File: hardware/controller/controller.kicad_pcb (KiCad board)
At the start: 2 copper layers, 64 x 39 mm, 13 parts, among them J1 Conn_01x02_Pin, J2 Conn_01x02_Pin, J3 Conn_01x02_Pin, J4 Conn_01x02_Pin, SW1 SW_DIP_x01, U1 ESP32-S3-DEVKITC-1-N8R8

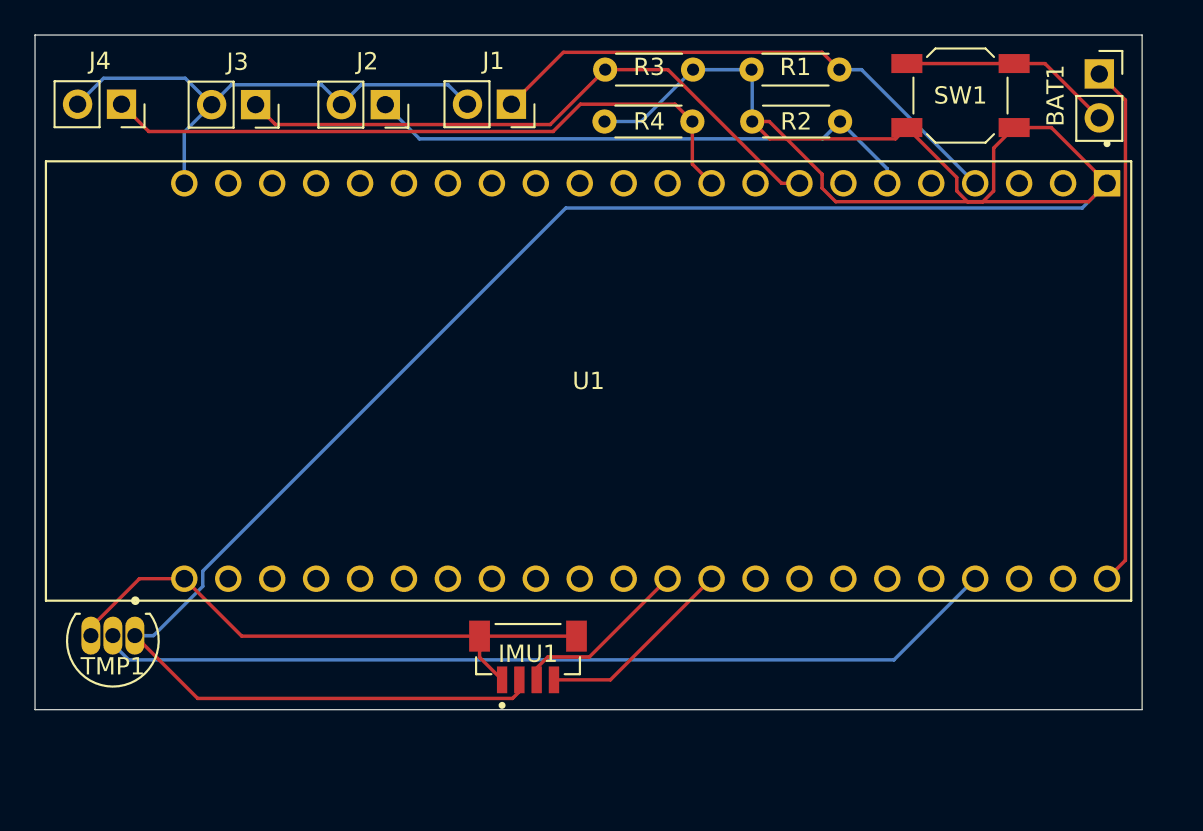
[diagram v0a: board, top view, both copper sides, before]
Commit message: PCB Redesign for UWB Module
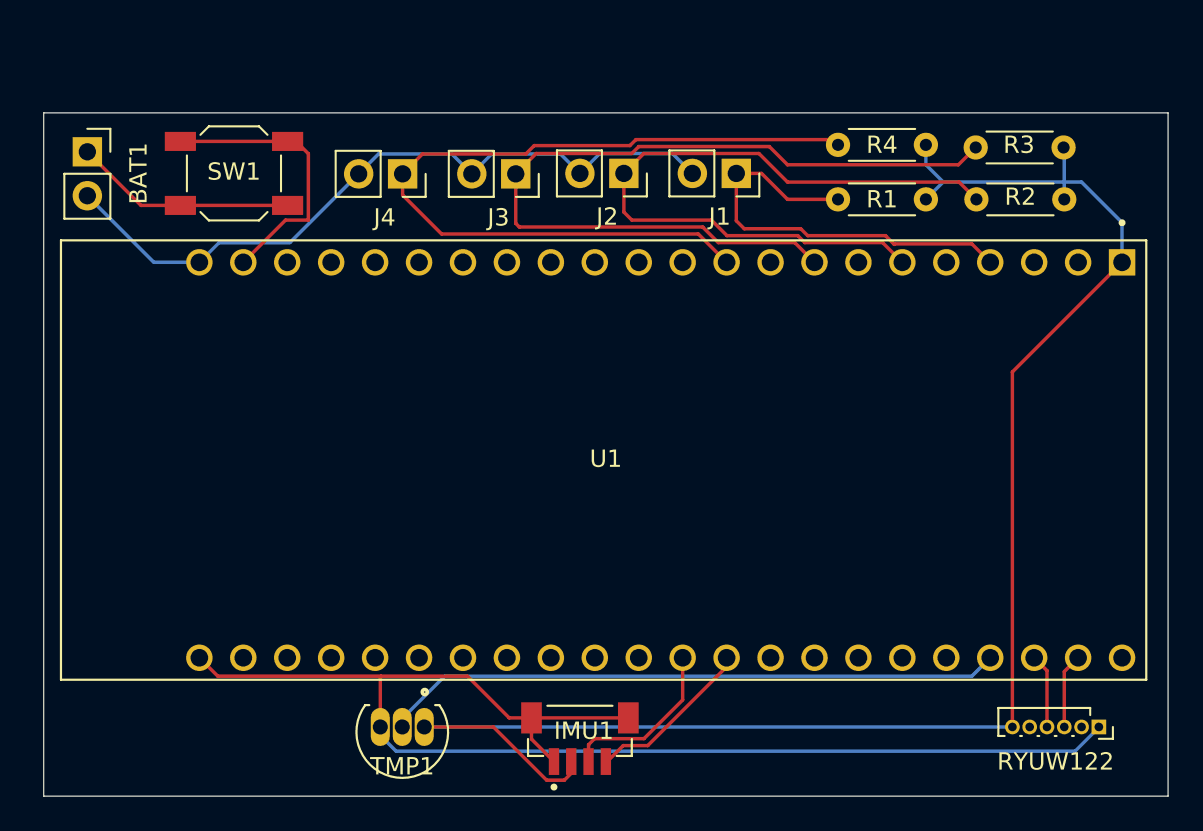
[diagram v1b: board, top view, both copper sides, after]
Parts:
- added RYUW122: Conn_01x06_Pin, Connector_PinSocket_1.00mm:PinSocket_1x06_P1.00mm_Vertical, F.Cu at (164.0, 134.5)
- moved BAT1 58.7 mm to (105.5, 101.2)
- moved SW1 42.2 mm to (114.0, 102.5)
- moved R3 21.9 mm to (162.0, 101.0)
- moved TMP1 17.5 mm to (123.7, 135.3)
- moved J4 16.7 mm to (123.8, 102.5)
- moved J3 15.6 mm to (130.3, 102.5)
- moved J2 14.4 mm to (136.5, 102.5)
- moved J1 13.6 mm to (143.0, 102.5)
- moved R2 9.07 mm to (156.9, 104.0), turned to 0 degrees
- moved R4 8.53 mm to (148.9, 100.8), turned to 0 degrees
- moved R1 7.50 mm to (148.9, 104.0), turned to 0 degrees
- moved IMU1 5.60 mm to (134.0, 134.7)
- moved U1 4.65 mm to (135.4, 119.1)
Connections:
- IMU1 pad 2: Net-(TMP1-+VS) -> Net-(RYUW122-Pin_6)
- J1 pad 2: GND -> Net-(BAT1-Pin_2)
- J2 pad 2: GND -> Net-(BAT1-Pin_2)
- J3 pad 2: GND -> Net-(BAT1-Pin_2)
- J4 pad 2: GND -> Net-(BAT1-Pin_2)
- R1 pad 2: Net-(TMP1-+VS) -> Net-(RYUW122-Pin_6)
- R2 pad 2: Net-(TMP1-+VS) -> Net-(RYUW122-Pin_6)
- R3 pad 1: Net-(TMP1-+VS) -> Net-(RYUW122-Pin_6)
- R4 pad 2: Net-(TMP1-+VS) -> Net-(RYUW122-Pin_6)
- SW1 pad 1: Net-(BAT1-Pin_2) -> Net-(U1-5V0)
- SW1 pad 2: Net-(TMP1-+VS) -> Net-(BAT1-Pin_1)
- TMP1 pad 1: Net-(TMP1-+VS) -> Net-(RYUW122-Pin_6)
- U1 pad J1_1: Net-(TMP1-+VS) -> Net-(RYUW122-Pin_6)
- U1 pad J1_21: unconnected-(U1-5V0-PadJ1_21) -> Net-(U1-5V0)
- U1 pad J1_22: GND -> Net-(BAT1-Pin_2)
- U1 pad J3_1: Net-(BAT1-Pin_1) -> unconnected-(U1-GND-PadJ3_1)
- U1 pad J3_2: unconnected-(U1-U0TXD/GPIO43-PadJ3_2) -> Net-(RYUW122-Pin_3)
- U1 pad J3_3: unconnected-(U1-U0RXD/GPIO44-PadJ3_3) -> Net-(RYUW122-Pin_4)
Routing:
- net Net-(TMP1-+VS): track 156.2 -> 0.00 mm
- net Net-(RYUW122-Pin_6): track 0.00 -> 94.7 mm
- net Net-(RYUW122-Pin_1): track 34.2 -> 75.3 mm
- net GND: track 30.9 -> 0.00 mm
- net Net-(BAT1-Pin_2): track 12.4 -> 41.5 mm
- net Net-(BAT1-Pin_1): track 30.2 -> 12.9 mm
- net Net-(TMP1-VOUT): track 52.7 -> 35.9 mm
- net Net-(U1-5V0): track 0.00 -> 16.3 mm
- net Net-(J3-Pin_1): track 36.0 -> 49.2 mm
- net Net-(J2-Pin_1): track 32.2 -> 41.5 mm
- net Net-(J4-Pin_1): track 38.8 -> 47.7 mm
- net Net-(J1-Pin_1): track 31.2 -> 24.9 mm
- net Net-(RYUW122-Pin_3): track 0.00 -> 4.33 mm
- net Net-(RYUW122-Pin_4): track 0.00 -> 4.31 mm
- net Net-(U1-GPIO38): track 11.5 -> 9.77 mm
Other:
- board size 64 x 39 mm -> 65 x 39.5 mm
